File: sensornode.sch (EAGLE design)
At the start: 72 parts, among them IC1 CP2104, Q1 mmbt2222, Q2 mmbt2222, Q3 DMG3415U, SW2 KMR2, U1 TSL2591, U2 AP2112-3.3, U3 MCP73831T-2ACI/OT, U4 BMEx80, X2 ESP32_WROOM32_SKINNY, X4 20329

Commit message: Getting the updates in
Yes, this is a terrible commit
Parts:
- C19: value 10uF -> 4.7uF
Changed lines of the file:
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@@
 <part name="U$43" library="microbuilder" deviceset="GND" device=""/>
 <part name="U1" library="microbuilder" deviceset="LIGHT_TSL2591" device="" value="TSL2591"/>
-<part name="C19" library="microbuilder" deviceset="CAP_CERAMIC" device="0805-NOOUTLINE" value="10uF"/>
+<part name="C19" library="microbuilder" deviceset="CAP_CERAMIC" device="0805-NOOUTLINE" value="4.7uF"/>
 <part name="U$32" library="microbuilder" deviceset="GND" device=""/>
 <part name="C20" library="microbuilder" deviceset="CAP_CERAMIC" device="0805-NOOUTLINE" value="10uF"/>

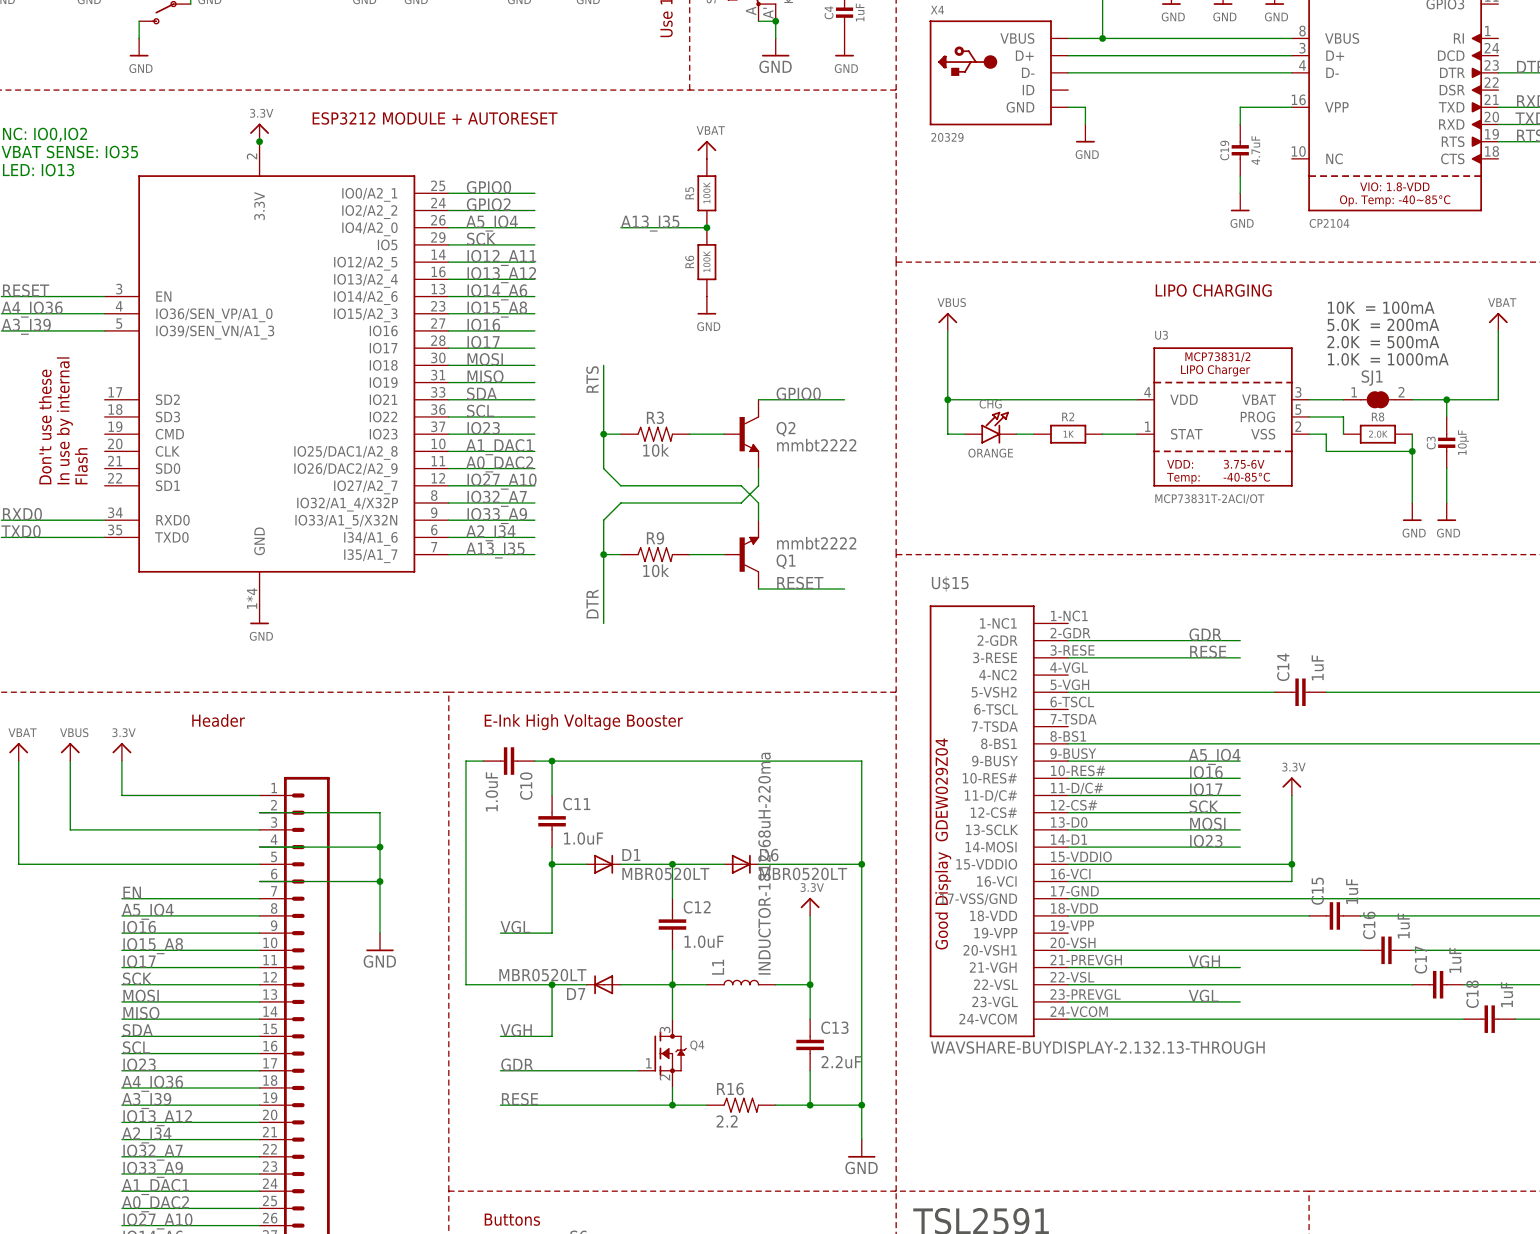
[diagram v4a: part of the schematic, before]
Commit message: Adjusting some signal names
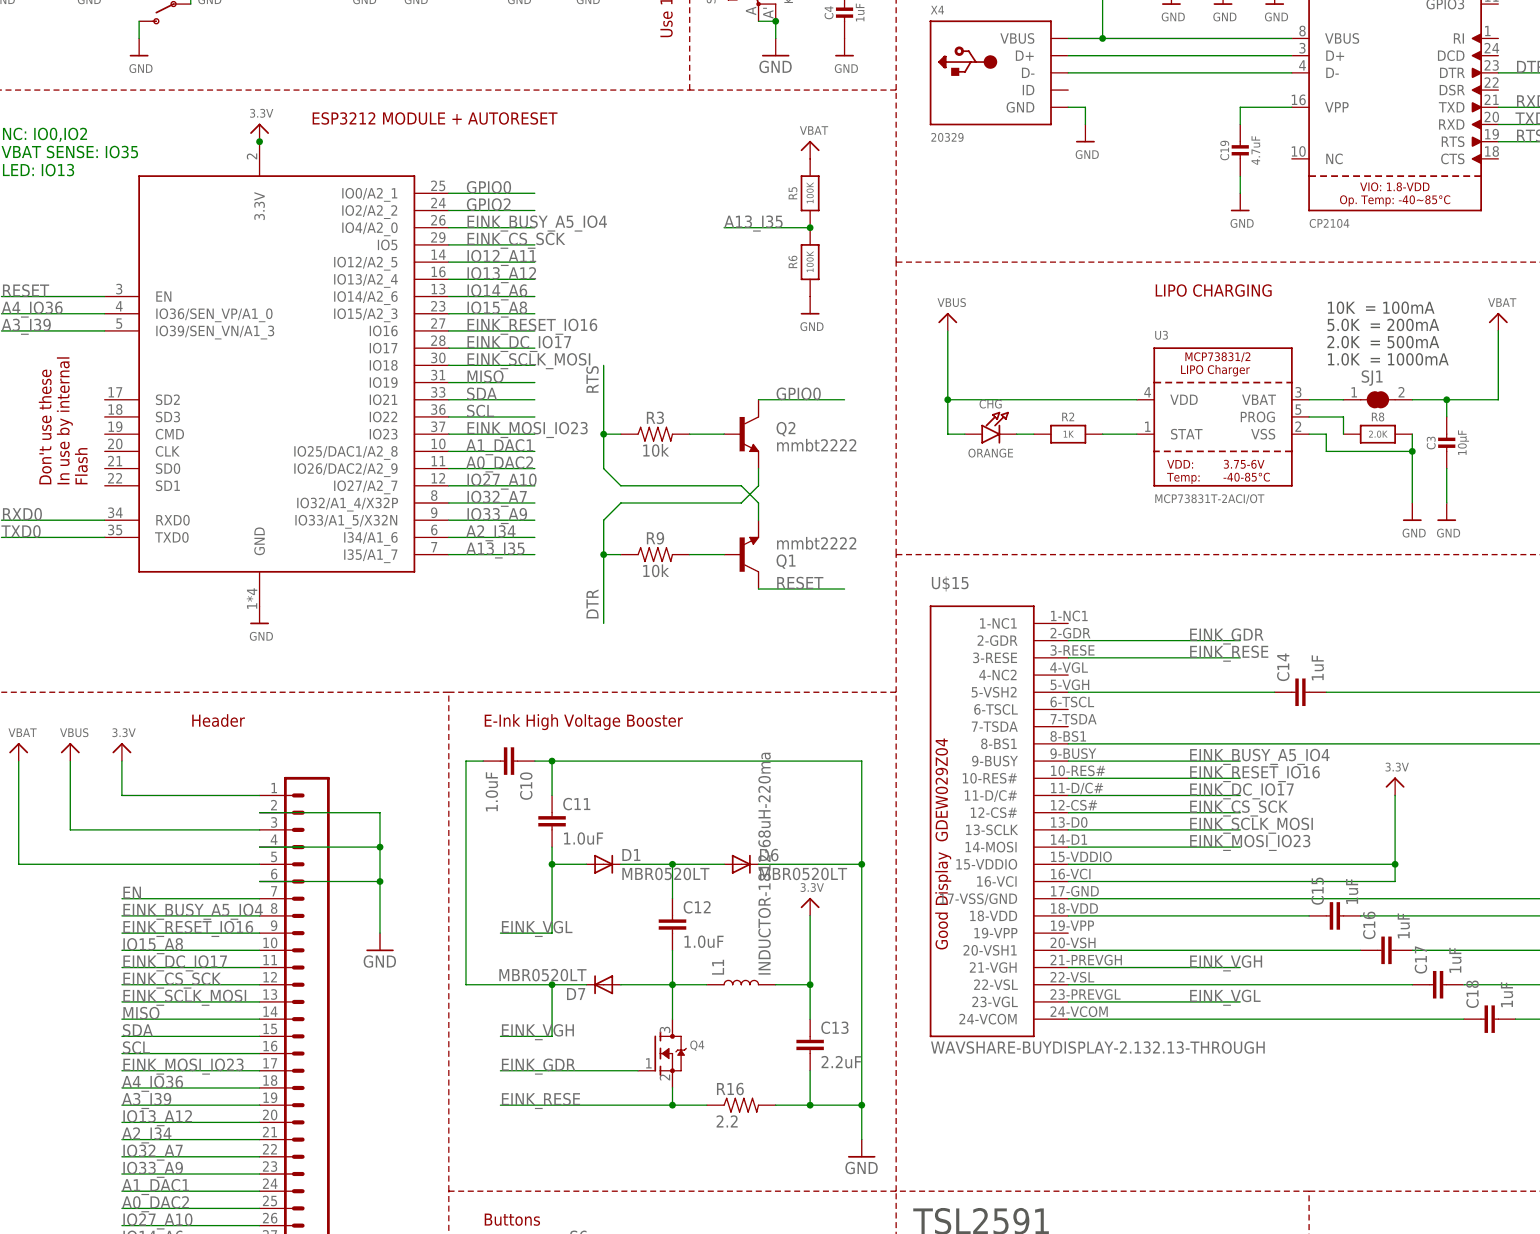
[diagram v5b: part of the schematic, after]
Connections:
- net A5_IO4 renamed EINK_BUSY_A5_IO4
- net GDR renamed EINK_GDR
- net IO16 renamed EINK_RESET_IO16
- net IO17 renamed EINK_DC_IO17
- net IO23 renamed EINK_MOSI_IO23
- net MOSI renamed EINK_SCLK_MOSI
- net RESE renamed EINK_RESE
- net SCK renamed EINK_CS_SCK
- net VGH renamed EINK_VGH
- net VGL renamed EINK_VGL
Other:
- moved on the sheet: R5, R6
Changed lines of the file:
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@@
 <instance part="U$37" gate="G$1" x="43.18" y="134.62"/>
 <instance part="X2" gate="G$1" x="43.18" y="165.1"/>
-<instance part="R5" gate="G$1" x="109.22" y="198.12" rot="R90"/>
-<instance part="R6" gate="G$1" x="109.22" y="187.96" rot="R90"/>
-<instance part="U$40" gate="G$1" x="109.22" y="205.74"/>
-<instance part="U$41" gate="G$1" x="109.22" y="180.34"/>
+<instance part="R5" gate="G$1" x="124.46" y="198.12" rot="R90"/>
+<instance part="R6" gate="G$1" x="124.46" y="187.96" rot="R90"/>
+<instance part="U$40" gate="G$1" x="124.46" y="205.74"/>
+<instance part="U$41" gate="G$1" x="124.46" y="180.34"/>
 <instance part="C4" gate="G$1" x="129.54" y="223.52"/>
 <instance part="U$42" gate="G$1" x="129.54" y="218.44"/>
@@
 <instance part="C14" gate="G$1" x="198.12" y="124.46" rot="R90"/>
 <instance part="U$19" gate="G$1" x="233.68" y="66.04"/>
-<instance part="U$20" gate="G$1" x="195.58" y="111.76"/>
+<instance part="U$20" gate="G$1" x="210.82" y="111.76"/>
 <instance part="C15" gate="G$1" x="203.2" y="91.44" rot="R90"/>
 <instance part="C16" gate="G$1" x="210.82" y="86.36" rot="R90"/>
@@
 <pinref part="U$15" gate="G$1" pin="15-VDDIO"/>
 <pinref part="U$20" gate="G$1" pin="3.3V"/>
-<wire x1="162.56" y1="99.06" x2="195.58" y2="99.06" width="0.1524" layer="91"/>
-<wire x1="195.58" y1="99.06" x2="195.58" y2="109.22" width="0.1524" layer="91"/>
+<wire x1="162.56" y1="99.06" x2="210.82" y2="99.06" width="0.1524" layer="91"/>
+<wire x1="210.82" y1="99.06" x2="210.82" y2="109.22" width="0.1524" layer="91"/>
 <pinref part="U$15" gate="G$1" pin="16-VCI"/>
-<wire x1="162.56" y1="96.52" x2="195.58" y2="96.52" width="0.1524" layer="91"/>
-<wire x1="195.58" y1="96.52" x2="195.58" y2="99.06" width="0.1524" layer="91"/>
-<junction x="195.58" y="99.06"/>
+<wire x1="162.56" y1="96.52" x2="210.82" y2="96.52" width="0.1524" layer="91"/>
+<wire x1="210.82" y1="96.52" x2="210.82" y2="99.06" width="0.1524" layer="91"/>
+<junction x="210.82" y="99.06"/>
 </segment>
 <segment>
@@
 </segment>
 </net>
-<net name="IO16" class="0">
+<net name="EINK_RESET_IO16" class="0">
 <segment>
 <wire x1="71.12" y1="177.8" x2="83.82" y2="177.8" width="0.1524" layer="91"/>
@@
 </segment>
 </net>
-<net name="IO17" class="0">
+<net name="EINK_DC_IO17" class="0">
 <segment>
 <wire x1="83.82" y1="175.26" x2="71.12" y2="175.26" width="0.1524" layer="91"/>
@@
 </segment>
 </net>
-<net name="MOSI" class="0">
+<net name="EINK_SCLK_MOSI" class="0">
 <segment>
 <wire x1="71.12" y1="172.72" x2="83.82" y2="172.72" width="0.1524" layer="91"/>
@@
 </segment>
 </net>
-<net name="A5_IO4" class="0">
+<net name="EINK_BUSY_A5_IO4" class="0">
 <segment>
 <wire x1="71.12" y1="193.04" x2="83.82" y2="193.04" width="0.1524" layer="91"/>
@@
 </segment>
 </net>
-<net name="IO23" class="0">
+<net name="EINK_MOSI_IO23" class="0">
 <segment>
 <wire x1="71.12" y1="162.56" x2="83.82" y2="162.56" width="0.1524" layer="91"/>
@@
 </segment>
 </net>
-<net name="SCK" class="0">
+<net name="EINK_CS_SCK" class="0">
 <segment>
 <wire x1="71.12" y1="190.5" x2="83.82" y2="190.5" width="0.1524" layer="91"/>
@@
 <pinref part="R5" gate="G$1" pin="1"/>
 <pinref part="R6" gate="G$1" pin="2"/>
-<wire x1="109.22" y1="193.04" x2="96.52" y2="193.04" width="0.1524" layer="91"/>
-<junction x="109.22" y="193.04"/>
-<label x="96.52" y="193.04" size="1.778" layer="95"/>
+<wire x1="124.46" y1="193.04" x2="111.76" y2="193.04" width="0.1524" layer="91"/>
+<junction x="124.46" y="193.04"/>
+<label x="111.76" y="193.04" size="1.778" layer="95"/>
 </segment>
 </net>
@@
 </segment>
 </net>
-<net name="VGL" class="0">
+<net name="EINK_VGL" class="0">
 <segment>
 <pinref part="C11" gate="G$1" pin="2"/>
@@
 </segment>
 </net>
-<net name="VGH" class="0">
+<net name="EINK_VGH" class="0">
 <segment>
 <pinref part="D7" gate="G$1" pin="C"/>
@@
 </segment>
 </net>
-<net name="GDR" class="0">
+<net name="EINK_GDR" class="0">
 <segment>
 <pinref part="Q4" gate="G$1" pin="G"/>
@@
 </segment>
 </net>
-<net name="RESE" class="0">
+<net name="EINK_RESE" class="0">
 <segment>
 <pinref part="Q4" gate="G$1" pin="S"/>
